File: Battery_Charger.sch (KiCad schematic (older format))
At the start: 51 parts, among them J1 OpenVent_Barrel_Connector, Q12 2N7002BK, Q8 SSM3K341R, U13 TLV7042DGKR, U14 LT3796, U16 TLV2333IDR

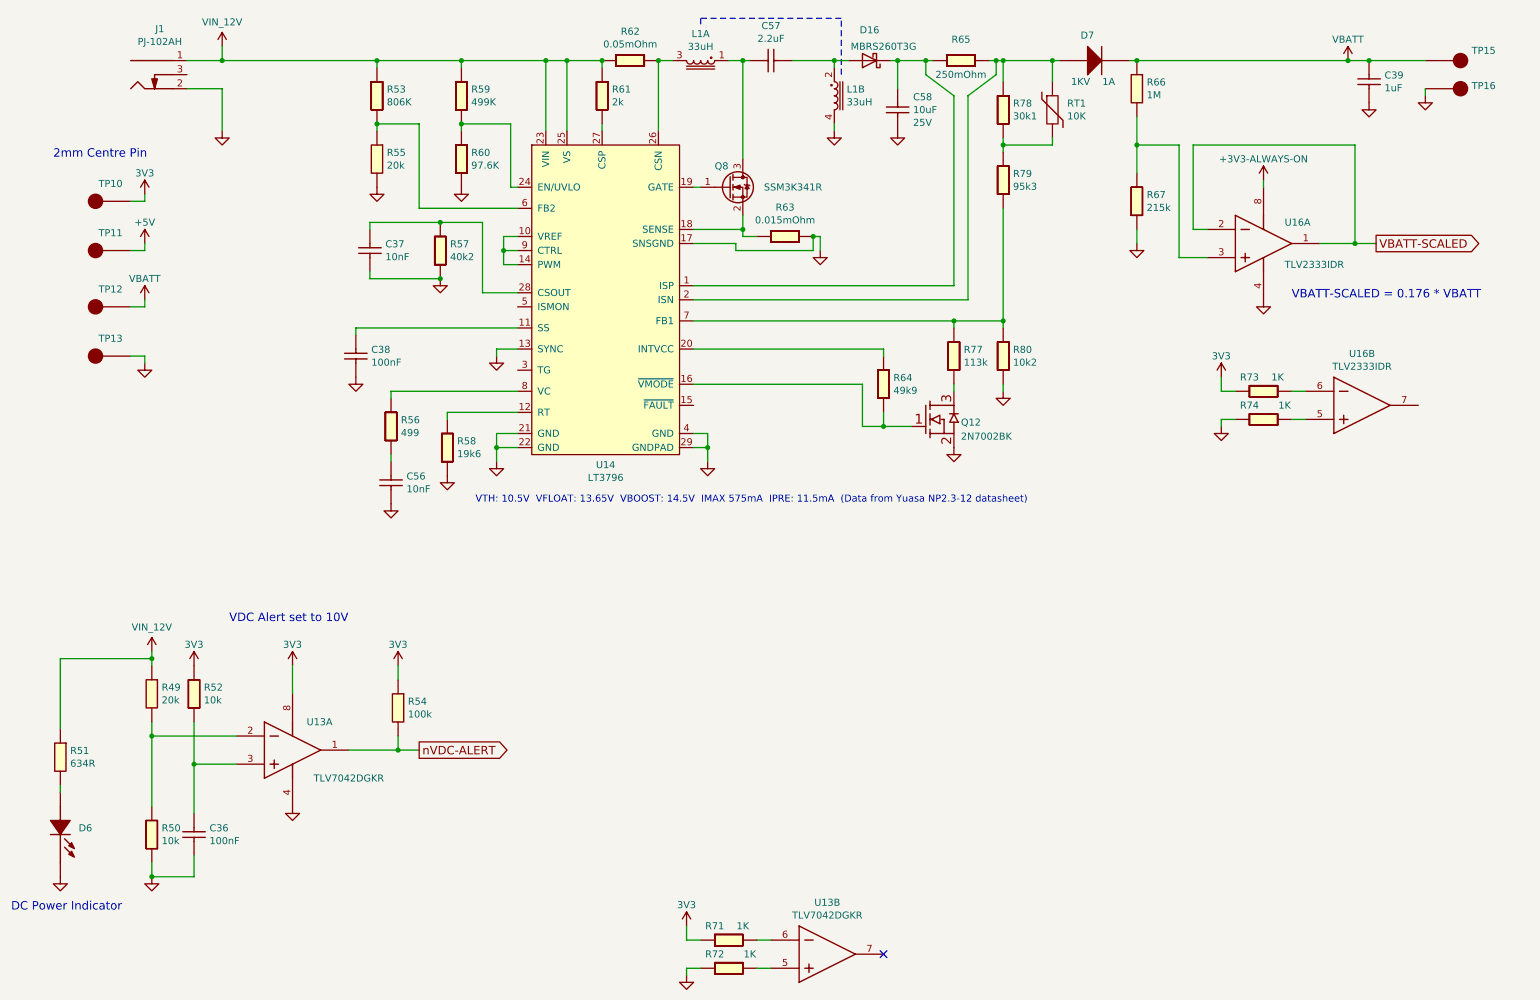
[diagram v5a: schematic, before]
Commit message: Split the design into two boards, main controller board and a power supply board.
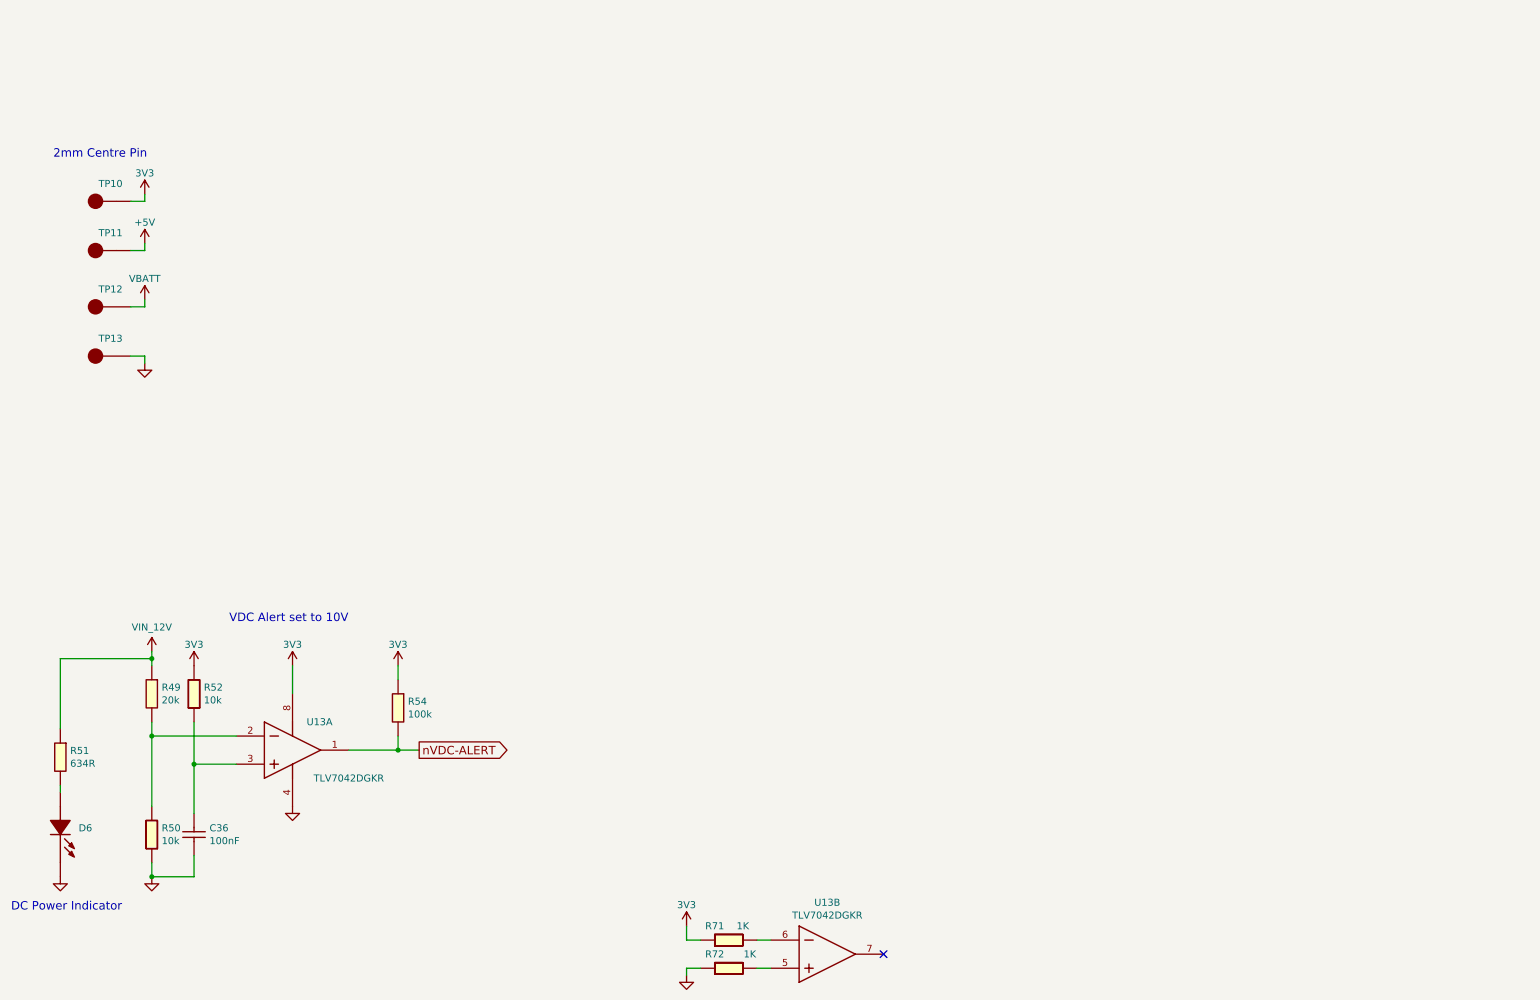
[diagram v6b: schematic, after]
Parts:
- removed C37, C56: 10nF_0603_Ceramic_Capacitor,_10%,_50V,_X7R-, symbol OpenVent:10nF_0603_Ceramic_Capacitor,_10%,_50V,_X7R-
- removed C38: 100nF_0603_Ceramic_Capacitor,_10%,_X7R,_25V, Capacitor_SMD:C_0603_1608Metric, symbol OpenVent:100nF_0603_Ceramic_Capacitor,_10%,_X7R,_25V
- removed C39: 1uF_0603_Ceramic_Capacitor,_10%,_50V,_X5R, Capacitor_SMD:C_0603_1608Metric, symbol OpenVent:1uF_0603_Ceramic_Capacitor,_10%,_50V,_X5R
- removed C57: 2.2uF_2824_film_capacitor_10%_40V, symbol OpenVent:2.2uF_2824_film_capacitor_10%_40V
- removed C58: C_1210_10uF_25V_10%_X7R, Capacitor_SMD:C_1210_3225Metric, symbol OpenVent:C_1210_10uF_25V_10%_X7R
- removed D16: MBRS260T3G, Diode_SMD:D_SMB, symbol OpenVent:MBRS260T3G
- removed D7: DIODE_GEN_PURP_1KV_1A_SMA, Diode_SMD:D_SMA, symbol OpenVent:DIODE_GEN_PURP_1KV_1A_SMA
- removed J1: OpenVent_Barrel_Connector, Connector_BarrelJack:BarrelJack_CUI_PJ-102AH_Horizontal, symbol OpenVent:OpenVent_Barrel_Connector
- removed L1: MSD1260-333, F_Inductors:MSD1260, symbol F_inductors:MSD1260-333
- removed Q12: 2N7002BK, Package_TO_SOT_SMD:SOT-23, symbol OpenVent:2N7002BK
- removed Q8: SSM3K341R, Package_TO_SOT_SMD:SOT-23, symbol OpenVent:SSM3K341R
- removed R53: R_0603_806K_0.1W_1%, symbol OpenVent:R_0603_806K_0.1W_1%
- removed R55: 20k_0603_Chip_Resistor,_1%,_0.1W, symbol OpenVent:20k_0603_Chip_Resistor,_1%,_0.1W
- removed R56: R_0603_499R_0.1W_1%, symbol OpenVent:R_0603_499R_0.1W_1%
- removed R57: R_0603_40k2K_0.1W_1%, symbol OpenVent:R_0603_40k2K_0.1W_1%
- removed R58: R_0603_19k6_0.1W_1%, symbol OpenVent:R_0603_19k6_0.1W_1%
- removed R59: R_0603_499K_0.1W_1%, symbol OpenVent:R_0603_499K_0.1W_1%
- removed R60: R_0603_97.6K_0.1W_1%, symbol OpenVent:R_0603_97.6K_0.1W_1%
- removed R61: R_0603_2k_0.1W_1%, symbol OpenVent:R_0603_2k_0.1W_1%
- removed R62: R_0805_050m_cursense, Resistor_SMD:R_0805_2012Metric, symbol OpenVent:R_0805_050m_cursense
- removed R63: R_0603_015m_cursense, Resistor_SMD:R_0603_1608Metric, symbol OpenVent:R_0603_015m_cursense
- removed R64: R_0603_49k9_0.1W_1%, symbol OpenVent:R_0603_49k9_0.1W_1%
- removed R65: R_1206_250m_cursense, Resistor_SMD:R_1206_3216Metric, symbol OpenVent:R_1206_250m_cursense
- removed R66: 1M_0603_Chip_Resistor,_1%,_0.1W, Resistor_SMD:R_0603_1608Metric, symbol OpenVent:1M_0603_Chip_Resistor,_1%,_0.1W
- removed R67: 215k_0603_Chip_Resistor,_1%,_0.1W, Resistor_SMD:R_0603_1608Metric, symbol OpenVent:215k_0603_Chip_Resistor,_1%,_0.1W
- removed R73, R74: 1K_0603_Chip_Resistor,_1%,_0.1W, Resistor_SMD:R_0603_1608Metric, symbol OpenVent:1K_0603_Chip_Resistor,_1%,_0.1W
- removed R77: R_0603_113k_0.1W_1%, symbol OpenVent:R_0603_113k_0.1W_1%
- removed R78: R_0603_30k1_0.1W_1%, symbol OpenVent:R_0603_30k1_0.1W_1%
- removed R79: R_0603_95k3_0.1W_1%, symbol OpenVent:R_0603_95k3_0.1W_1%
- removed R80: R_0603_10k2_0.1W_1%, symbol OpenVent:R_0603_10k2_0.1W_1%
- removed RT1: R_Thermistor_0603_10K_NTC, Resistor_SMD:R_0603_1608Metric, symbol OpenVent:R_Thermistor_0603_10K_NTC
- removed TP15, TP16: Test_Point_PTH, TestPoint:TestPoint_Pad_2.0x2.0mm, symbol OpenVent:Test_Point_PTH
- removed U14: LT3796, F_ICs:TSSOP-28-LTvar_EB_4.4x9.7mm_P0.65mm, symbol F_ICs:LT3796
- removed U16: TLV2333IDR, Package_SO:SOIC-8_3.9x4.9mm_P1.27mm, symbol OpenVent:TLV2333IDR
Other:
- note removed: "VBATT-SCALED = 0.176 * VBATT"
- note removed: "VTH: 10.5V VFLOAT: 13.65V VBOOST: 14.5V IMAX 575mA IPRE: 11.5mA (Data from Yuasa NP2.3-12 datasheet)"

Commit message: Sorted out the interconnect between power supply and main boards.
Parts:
- removed C36: 100nF_0603_Ceramic_Capacitor,_10%,_X7R,_25V, Capacitor_SMD:C_0603_1608Metric, symbol OpenVent:100nF_0603_Ceramic_Capacitor,_10%,_X7R,_25V
- removed D6: LED_GREEN_0603_SMD, LED_SMD:LED_0603_1608Metric, symbol OpenVent:LED_GREEN_0603_SMD
- removed R49: 20k_0603_Chip_Resistor,_1%,_0.1W, Resistor_SMD:R_0603_1608Metric, symbol OpenVent:20k_0603_Chip_Resistor,_1%,_0.1W
- removed R50, R52: 10k_0603_Chip_Resistor,_1%,_0.1W, Resistor_SMD:R_0603_1608Metric, symbol OpenVent:10k_0603_Chip_Resistor,_1%,_0.1W
- removed R51: 634R_0603_Chip_Resistor,_1%,_0.1W, Resistor_SMD:R_0603_1608Metric, symbol OpenVent:634R_0603_Chip_Resistor,_1%,_0.1W
- removed R54: 100K_0603_Chip_Resistor,_1%,_0.1W, Resistor_SMD:R_0603_1608Metric, symbol OpenVent:100K_0603_Chip_Resistor,_1%,_0.1W
- removed R71, R72: 1K_0603_Chip_Resistor,_1%,_0.1W, Resistor_SMD:R_0603_1608Metric, symbol OpenVent:1K_0603_Chip_Resistor,_1%,_0.1W
- removed TP10, TP11, TP12, TP13: Test_Point_PTH, TestPoint:TestPoint_Pad_2.0x2.0mm, symbol OpenVent:Test_Point_PTH
- removed U13: TLV7042DGKR, Package_SO:VSSOP-8_3.0x3.0mm_P0.65mm, symbol OpenVent:TLV7042DGKR
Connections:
- no-connect marks 1 -> 0
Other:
- note removed: "2mm Centre Pin"
- note removed: "DC Power Indicator"
- note removed: "VDC Alert set to 10V"
